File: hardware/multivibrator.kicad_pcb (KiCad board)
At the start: 2 copper layers, 17 x 35 mm, 9 parts, among them J1 KLS2-EDR-5.08-02P-4, Q1 BC817, Q2 BC817

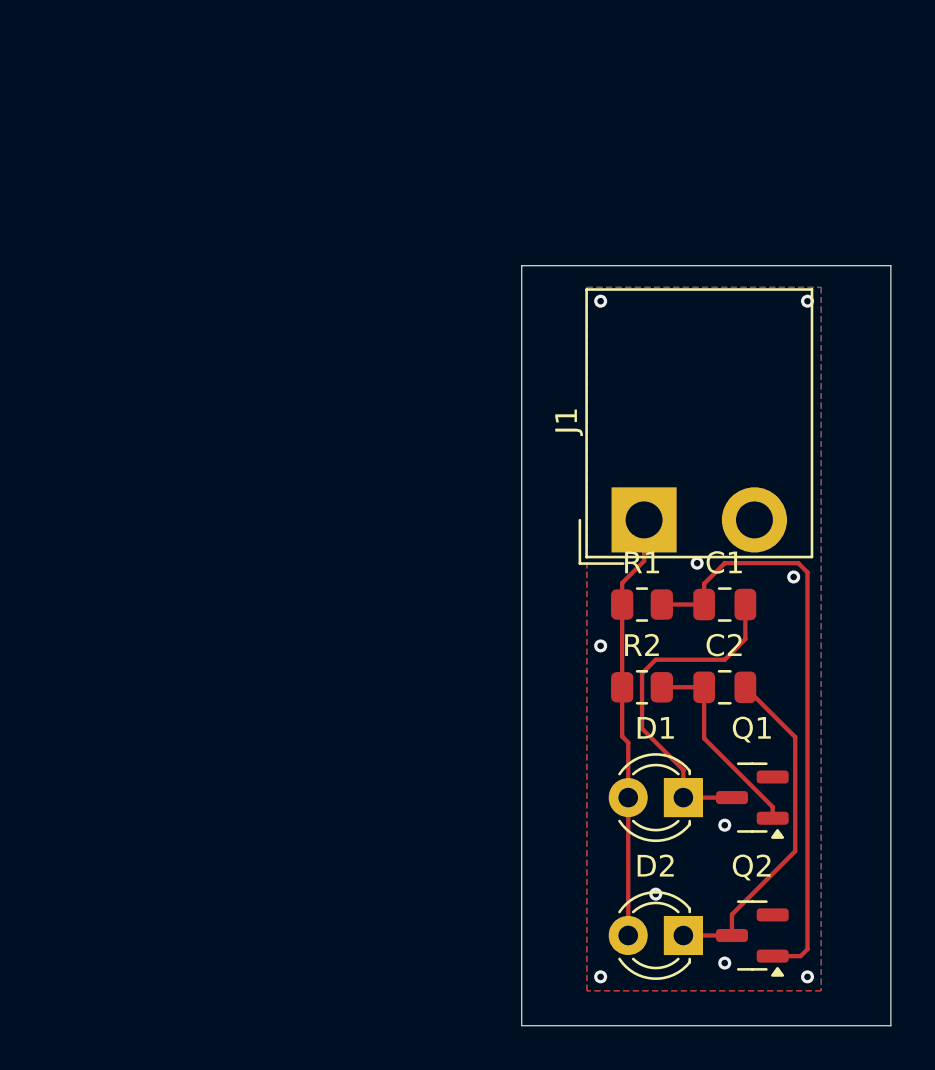
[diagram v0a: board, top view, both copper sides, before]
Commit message: Добавлены монтажные отверстия
+ изменена структура репозитория
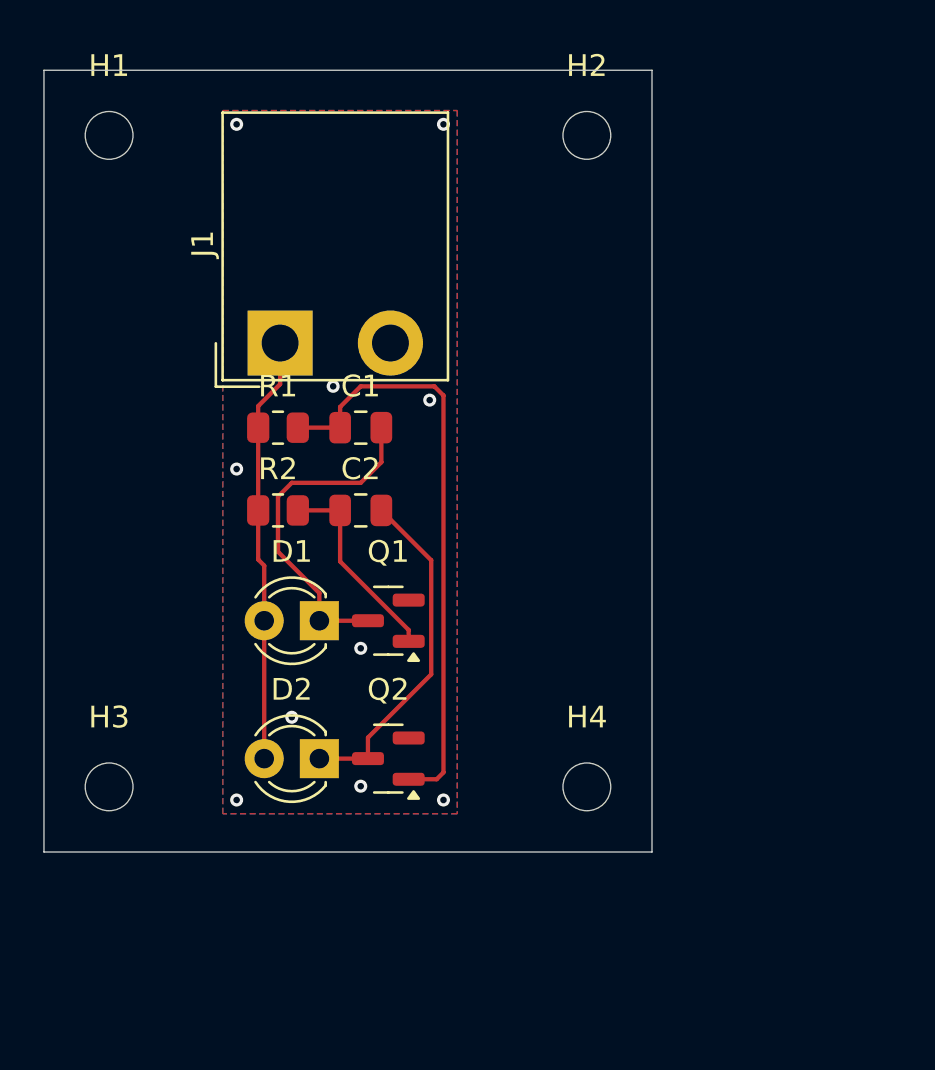
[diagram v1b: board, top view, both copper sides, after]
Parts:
- added H1: MountingHole, MountingHole:MountingHole_2.2mm_M2, F.Cu at (28.0, 33.0)
- added H2: MountingHole, MountingHole:MountingHole_2.2mm_M2, F.Cu at (50.0, 33.0)
- added H3: MountingHole, MountingHole:MountingHole_2.2mm_M2, F.Cu at (28.0, 63.0)
- added H4: MountingHole, MountingHole:MountingHole_2.2mm_M2, F.Cu at (50.0, 63.0)
- moved J1 18.6 mm to (35.9, 42.6)
- moved C1 18.6 mm to (39.6, 46.5)
- moved C2 18.6 mm to (39.6, 50.3)
- moved D1 18.6 mm to (37.7, 55.4)
- moved D2 18.6 mm to (37.7, 61.7)
- moved Q1 18.6 mm to (40.9, 55.4)
- moved Q2 18.6 mm to (40.9, 61.7)
- moved R1 18.6 mm to (35.8, 46.5)
- moved R2 18.6 mm to (35.8, 50.3)
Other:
- board size 17 x 35 mm -> 28 x 36 mm

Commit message: учтены замечания
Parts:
- H1, H2, H3, H4: value MountingHole -> MountingHole_Pad; footprint MountingHole:MountingHole_2.2mm_M2 -> MountingHole:MountingHole_3.2mm_M3_DIN965_Pad
- moved H1 5.99 mm to (33.8, 34.4)
- moved Q1 5.95 mm to (46.8, 55.4)
- moved Q2 5.95 mm to (46.8, 61.7)
- moved H3 5.94 mm to (33.8, 61.8)
- moved C1 5.33 mm to (44.9, 46.5)
- moved C2 5.33 mm to (44.9, 50.3)
- moved D1 5.33 mm to (43.0, 55.4)
- moved D2 5.33 mm to (43.0, 61.7)
- moved J1 5.33 mm to (41.2, 42.6)
- moved R1 5.33 mm to (41.1, 46.5)
- moved R2 5.33 mm to (41.1, 50.3)
- moved H2 4.38 mm to (54.1, 34.4)
- moved H4 4.32 mm to (54.1, 61.8)
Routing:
- net Net-(D1-K): track 15.7 -> 11.1 mm, vias 0 -> 2
- net Net-(D2-K): track 15.8 -> 20.2 mm
- net Net-(Q1-B): track 9.29 -> 13.1 mm
- net Net-(Q2-B): track 28.0 -> 26.1 mm
- net +5V: track 19.7 -> 21.1 mm
- net GND: vias 10 -> 9

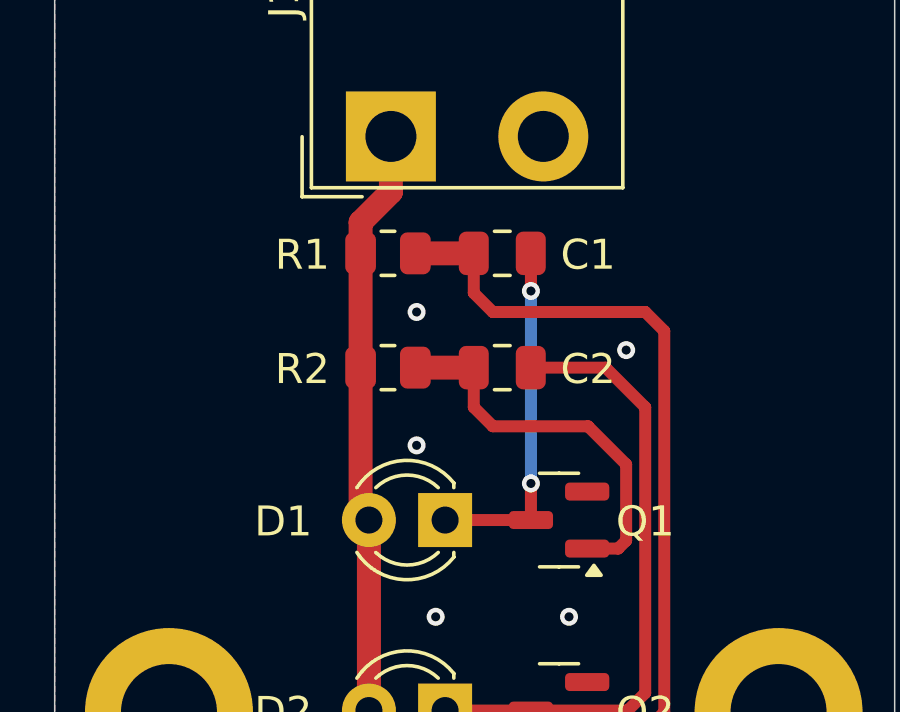
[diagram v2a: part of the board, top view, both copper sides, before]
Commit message: приняты новые рекомендации
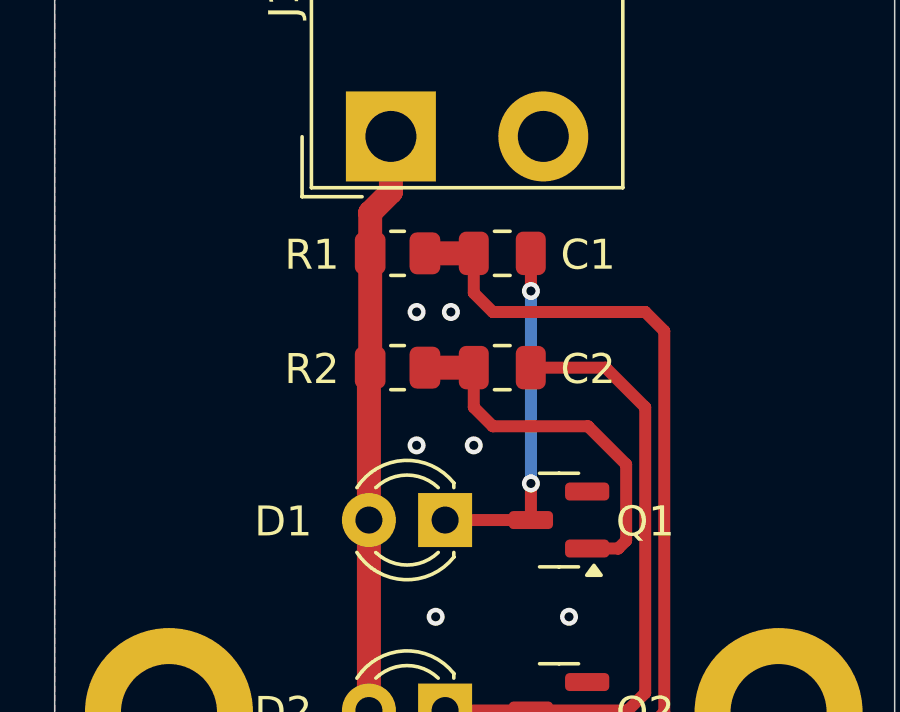
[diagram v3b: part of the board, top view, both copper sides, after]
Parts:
- C1, C2: value 50u -> 47u
- moved R1 0.32 mm to (41.4, 46.5)
- moved R2 0.32 mm to (41.4, 50.3)
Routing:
- net GND: vias 9 -> 10
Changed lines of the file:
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@@
 			(outputformat 1)
 			(mirror no)
-			(drillshape 1)
+			(drillshape 0)
 			(scaleselection 1)
-			(outputdirectory "")
+			(outputdirectory "../manufacturing/gerber/")
 		)
 	)
@@
 			)
 		)
+		(property "chipdip" "8023113118"
+			(at 0 0 180)
+			(unlocked yes)
+			(layer "F.Fab")
+			(hide yes)
+			(effects
+				(font
+					(size 1 1)
+					(thickness 0.15)
+				)
+			)
+		)
 		(property ki_fp_filters "LED*3.0mm*IRBlack*")
 		(sheetname "Корневой лист")
@@
 			)
 		)
-		(property "Value" "50u"
+		(property "Value" "47u"
 			(at 0 1.68 0)
 			(layer "F.Fab")
@@
 			)
 		)
-		(property "chipdip" ""
+		(property "chipdip" "9000326168"
 			(at 0 0 180)
 			(unlocked yes)
@@
 			)
 		)
-		(property "chipdip" ""
+		(property "chipdip" "28806907"
 			(at 0 0 180)
 			(unlocked yes)
@@
 	(footprint "Resistor_SMD:R_0805_2012Metric"
 		(layer "F.Cu")
-		(at 41.11 46.46)
+		(at 41.43 46.46)
 		(descr "Resistor SMD 0805 (2012 Metric), square (rectangular) end terminal, IPC_7351 nominal, (Body size source: IPC-SM-782 page 72, https://www.pcb-3d.com/wordpress/wp-content/uploads/ipc-sm-782a_amendment_1_and_2.pdf), generated with kicad-footprint-generator")
 		(tags "resistor")
@@
 			)
 		)
-		(property "chipdip" ""
+		(property "chipdip" "9000189877"
 			(at 0 0 0)
 			(unlocked yes)
@@
 			)
 		)
-		(property "Value" "50u"
+		(property "Value" "47u"
 			(at 0 1.68 0)
 			(layer "F.Fab")
@@
 			)
 		)
-		(property "chipdip" ""
+		(property "chipdip" "9000326168"
 			(at 0 0 0)
 			(unlocked yes)
@@
 			)
 		)
-		(property "chipdip" ""
+		(property "chipdip" "9000603329"
 			(at 0 0 90)
 			(unlocked yes)
@@
 			)
 		)
-		(property "chipdip" ""
+		(property "chipdip" "28806907"
 			(at 0 0 180)
 			(unlocked yes)
@@
 			)
 		)
+		(property "chipdip" "8023113118"
+			(at 0 0 180)
+			(unlocked yes)
+			(layer "F.Fab")
+			(hide yes)
+			(effects
+				(font
+					(size 1 1)
+					(thickness 0.15)
+				)
+			)
+		)
 		(property ki_fp_filters "LED*3.0mm*IRBlack*")
 		(sheetname "Корневой лист")
@@
 	(footprint "Resistor_SMD:R_0805_2012Metric"
 		(layer "F.Cu")
-		(at 41.11 50.27)
+		(at 41.43 50.27)
 		(descr "Resistor SMD 0805 (2012 Metric), square (rectangular) end terminal, IPC_7351 nominal, (Body size source: IPC-SM-782 page 72, https://www.pcb-3d.com/wordpress/wp-content/uploads/ipc-sm-782a_amendment_1_and_2.pdf), generated with kicad-footprint-generator")
 		(tags "resistor")
@@
 			)
 		)
-		(property "chipdip" ""
+		(property "chipdip" "9000189877"
 			(at 0 0 0)
 			(unlocked yes)
@@
 	)
 	(segment
-		(start 50.32 61.75)
-		(end 50.32 49.05)
-		(width 0.4)
+		(start 42.3425 46.46)
+		(end 43.97 46.46)
+		(width 0.8)
 		(layer "F.Cu")
 		(net 1)
 	)
 	(segment
-		(start 42.0225 46.46)
-		(end 43.97 46.46)
-		(width 0.8)
+		(start 50.32 61.75)
+		(end 50.32 49.05)
+		(width 0.4)
 		(layer "F.Cu")
 		(net 1)
@@
 	)
 	(segment
+		(start 42.3425 50.27)
+		(end 43.97 50.27)
+		(width 0.8)
+		(layer "F.Cu")
+		(net 4)
+	)
+	(segment
 		(start 48.785 56.3)
 		(end 49.05 56.035)
@@
 	)
 	(segment
-		(start 42.0225 50.27)
-		(end 43.97 50.27)
-		(width 0.8)
-		(layer "F.Cu")
-		(net 4)
-	)
-	(segment
 		(start 43.97 51.59)
 		(end 43.97 50.27)
@@
 	)
 	(segment
-		(start 40.1975 50.27)
-		(end 40.1975 55.0725)
+		(start 41.2075 42.5625)
+		(end 40.1975 43.5725)
 		(width 0.8)
 		(layer "F.Cu")
@@
 	)
 	(segment
-		(start 40.1975 46.46)
-		(end 40.1975 45.425)
+		(start 40.5175 45.105)
+		(end 41.2075 44.415)
 		(width 0.8)
 		(layer "F.Cu")
@@
 	)
 	(segment
-		(start 40.1975 50.27)
-		(end 40.1975 46.46)
+		(start 40.1975 55.0725)
+		(end 40.475 55.35)
 		(width 0.8)
 		(layer "F.Cu")
@@
 	)
 	(segment
-		(start 41.2075 42.5625)
-		(end 40.1975 43.5725)
+		(start 40.475 55.35)
+		(end 40.475 50.3125)
 		(width 0.8)
 		(layer "F.Cu")
@@
 	)
 	(segment
-		(start 40.1975 55.0725)
-		(end 40.475 55.35)
+		(start 40.5175 46.46)
+		(end 40.5175 45.105)
 		(width 0.8)
 		(layer "F.Cu")
@@
 	)
 	(segment
-		(start 41.2075 44.415)
-		(end 41.2075 42.5625)
+		(start 40.475 50.3125)
+		(end 40.5175 50.27)
 		(width 0.8)
 		(layer "F.Cu")
@@
 	)
 	(segment
-		(start 40.1975 45.425)
-		(end 41.2075 44.415)
+		(start 41.2075 44.415)
+		(end 41.2075 42.5625)
+		(width 0.8)
+		(layer "F.Cu")
+		(net 5)
+	)
+	(segment
+		(start 40.5175 50.27)
+		(end 40.5175 46.46)
 		(width 0.8)
 		(layer "F.Cu")
@@
 	)
 	(via
+		(at 42.065 48.415)
+		(size 0.6)
+		(drill 0.3)
+		(layers "F.Cu" "B.Cu")
+		(free yes)
+		(net 6)
+	)
+	(via
 		(at 42.7 58.575)
 		(size 0.6)
@@
 	)
 	(via
-		(at 56.67 31.27)
+		(at 43.97 52.86)
 		(size 0.6)
 		(drill 0.3)
@@
 	)
 	(via
-		(at 31.27 64.925)
+		(at 56.67 31.27)
 		(size 0.6)
 		(drill 0.3)
@@
 	)
 	(via
-		(at 42.065 52.86)
+		(at 31.27 64.925)
 		(size 0.6)
 		(drill 0.3)
@@
 	)
 	(via
-		(at 49.05 49.685)
+		(at 42.065 52.86)
 		(size 0.6)
 		(drill 0.3)
@@
 	)
 	(via
-		(at 42.065 48.415)
+		(at 43.208 48.415)
 		(size 0.6)
 		(drill 0.3)
@@
 		(hatch edge 0.5)
 		(connect_pads
-			(clearance 0.5)
+			(clearance 0.2)
 		)
 		(min_thickness 0.25)
